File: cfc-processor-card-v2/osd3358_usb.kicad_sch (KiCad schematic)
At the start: 33 parts, among them U7 OSD3358-512M-BSM, Y1 24MHz, Y2 ABS07-32.768KHZ-T

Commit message: Clean up CFC Processor Card from Scott's initial import which was Gerber identical to origianl EAGLE schematic. Interestingly, this version was already changed for the v2 backplane which is great. Align schematic to be more KiCAD like based off of the C3, rename a few things, remove some outdated OPD connections, import sch into pcb, clean up pcb detritus, and import DRU settings. No longer Gerber identicial, but it's now ready for further polishing for fabrication.
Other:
- note removed: "1.2"
- note removed: "OreSat Star Tracker: USB, JTAG, OSC"
- company: (none) -> Portland State Aerospace Society
- title: (none) -> OreSat CFC Processor Card
- moved on the sheet: C19, C22, C29, C30, C50, C51, FB2, R13, R21, R27, TP10, TP11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

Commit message: more trace polishing.
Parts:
- C19, C22, C29, C30, C50, C51, R13, R21, R27: footprint cfc-card:.0603-A -> oresat-passives:0603-C-NOSILK
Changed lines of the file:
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@@
 			)
 		)
-		(property "Footprint" "cfc-card:.0603-A"
+		(property "Footprint" "oresat-passives:0603-C-NOSILK"
 			(at 153.67 80.01 0)
 			(effects
@@
 			)
 		)
-		(property "Footprint" "cfc-card:.0603-A"
+		(property "Footprint" "oresat-passives:0603-C-NOSILK"
 			(at 128.27 87.63 0)
 			(effects
@@
 			)
 		)
-		(property "Footprint" "cfc-card:.0603-A"
+		(property "Footprint" "oresat-passives:0603-C-NOSILK"
 			(at 135.89 118.11 0)
 			(effects
@@
 			)
 		)
-		(property "Footprint" "cfc-card:.0603-A"
+		(property "Footprint" "oresat-passives:0603-C-NOSILK"
 			(at 313.69 102.87 0)
 			(effects
@@
 			)
 		)
-		(property "Footprint" "cfc-card:.0603-A"
+		(property "Footprint" "oresat-passives:0603-C-NOSILK"
 			(at 135.89 102.87 0)
 			(effects
@@
 			)
 		)
-		(property "Footprint" "cfc-card:.0603-A"
+		(property "Footprint" "oresat-passives:0603-C-NOSILK"
 			(at 252.73 87.63 0)
 			(effects
@@
 			)
 		)
-		(property "Footprint" "cfc-card:.0603-A"
+		(property "Footprint" "oresat-passives:0603-C-NOSILK"
 			(at 158.75 110.49 0)
 			(effects
@@
 			)
 		)
-		(property "Footprint" "cfc-card:.0603-A"
+		(property "Footprint" "oresat-passives:0603-C-NOSILK"
 			(at 128.27 72.39 0)
 			(effects
@@
 			)
 		)
-		(property "Footprint" "cfc-card:.0603-A"
+		(property "Footprint" "oresat-passives:0603-C-NOSILK"
 			(at 313.69 95.25 0)
 			(effects

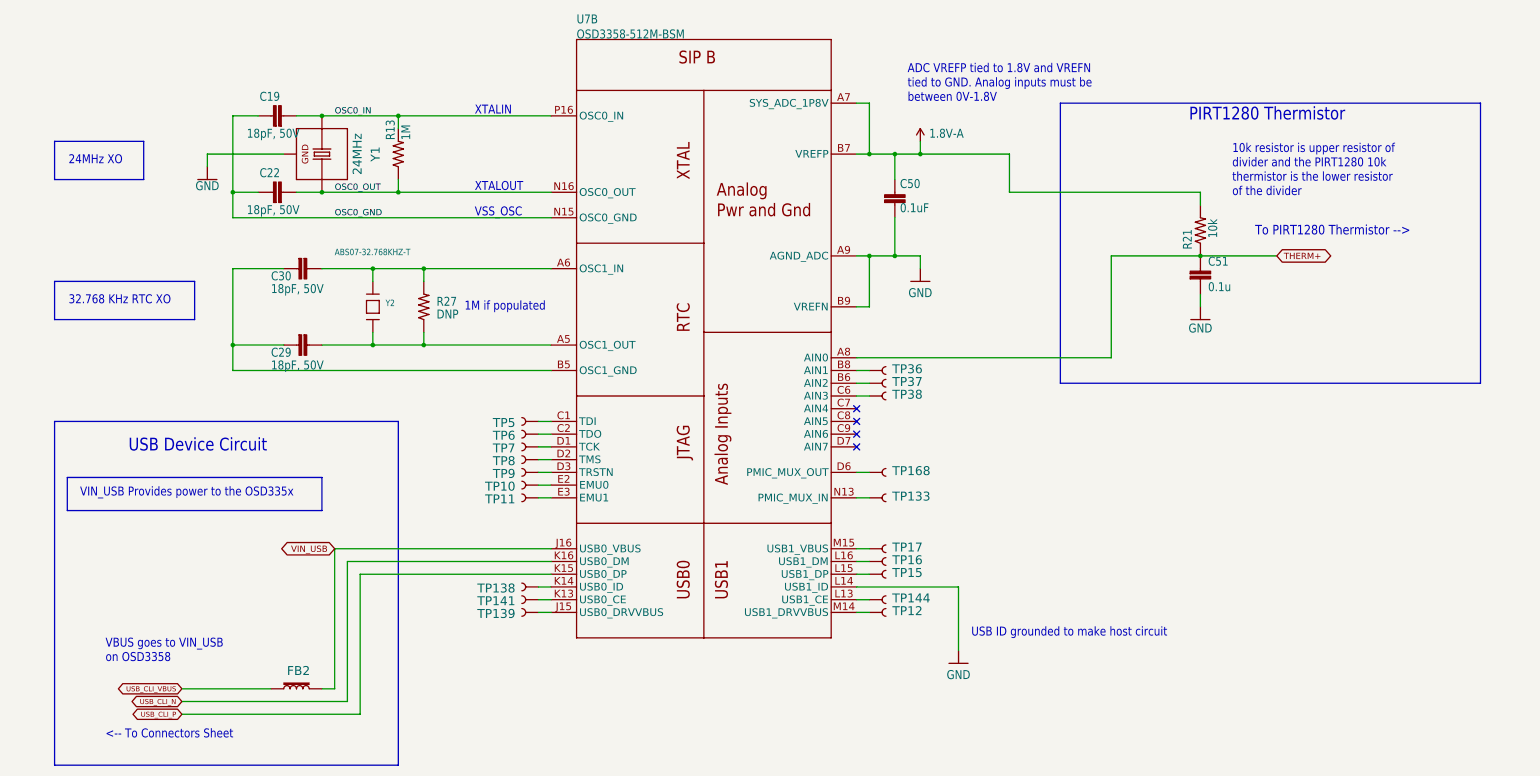
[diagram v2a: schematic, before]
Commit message: Final polish on schematic and PCB. Cleaned up BOM, fixed github issues which were not really issues. Lots of BOM cleanup, with MPNs and DPNs.
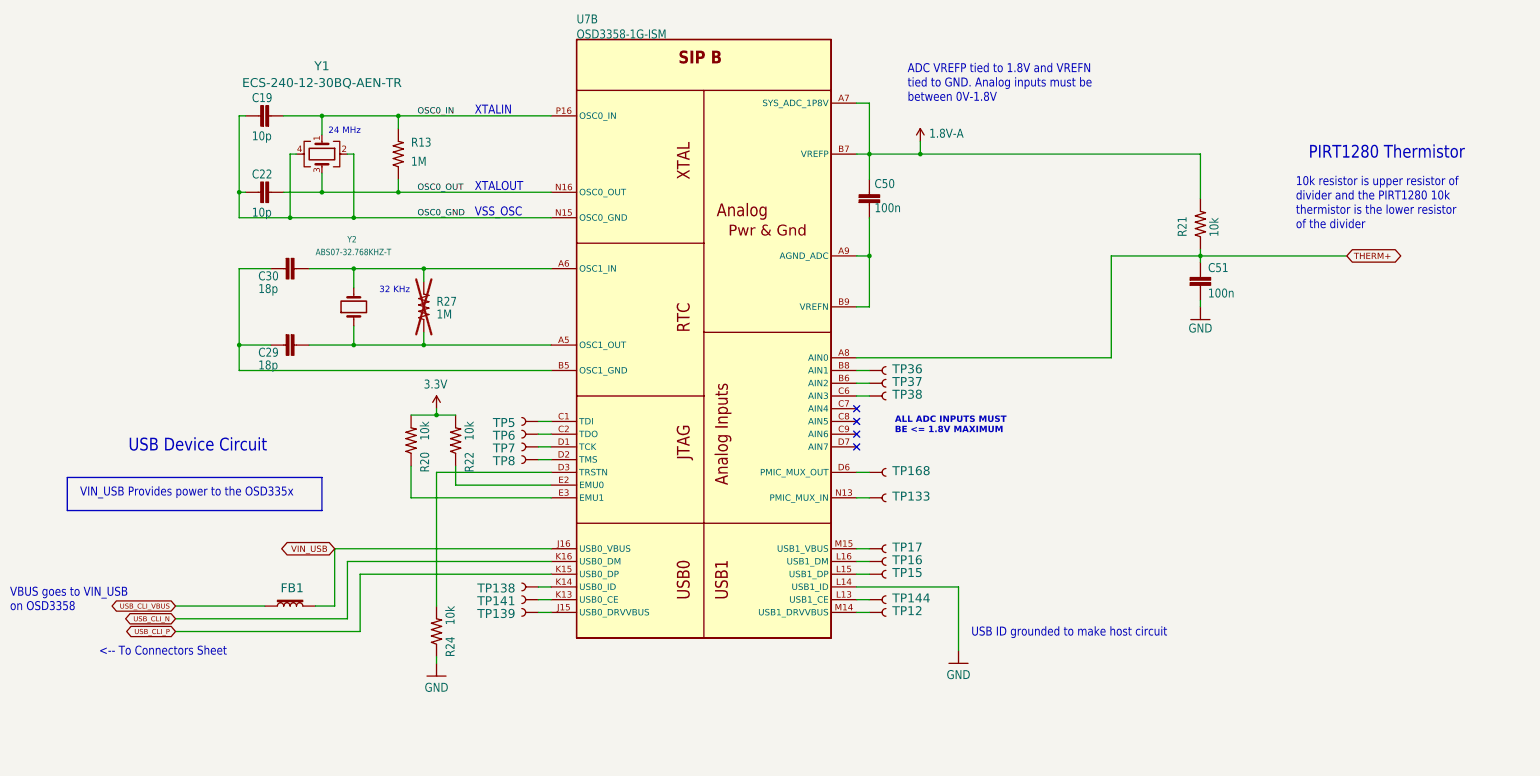
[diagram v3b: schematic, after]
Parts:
- removed TP10, TP11, TP9: TEST-POINT3X4, cfc-card:PAD.03X.04, symbol cfc-card-eagle-import:TEST-POINT3X4
- added R20, R22, R24: 10k, oresat-passives:0603-C-NOSILK, symbol cfc-card-eagle-import:R-US_0603-A
- C19, C22: value 18pF, 50V -> 10p; DIS (none) -> DigiKey; DPN (none) -> 399-6840-1-ND; MFR (none) -> KEMET; MPN (none) -> C0603C100J5GACAUTO
- C29, C30: value 18pF, 50V -> 18p; DIS (none) -> DigiKey; DPN (none) -> 399-C0603C180F5GACAUTOCT-ND; MFR (none) -> KEMET; MPN (none) -> C0603C180F5GACAUTO
- C50: value 0.1uF -> 100n; DIS (none) -> DigiKey; DPN (none) -> 587-3472-1-ND; MFR (none) -> Taiyo Yuden; MPN (none) -> TMK107BJ104KAHT
- C51: value 0.1u -> 100n; DIS (none) -> DigiKey; DPN (none) -> 587-3472-1-ND; MFR (none) -> Taiyo Yuden; MPN (none) -> TMK107BJ104KAHT
- FB1: renamed from FB2; value 30Ω/1.8A -> BLM18KG300JH1D; footprint cfc-card:0603 -> Inductor_SMD:L_0603_1608Metric; DIS (none) -> DigiKey; MFR (none) -> Murata Electronics
- R13: DIS (none) -> DigiKey; DPN (none) -> RMCF0603FG1M00CT-ND; MFR (none) -> Stackpole Electronics Inc; MPN (none) -> RMCF0603FG1M00
- R21: DIS (none) -> DigiKey; DPN (none) -> RMCF0603FT10K0CT-ND; MFR (none) -> Stackpole Electronics Inc; MPN (none) -> RMCF0603FT10K0
- R27: value DNP -> 1M; now not fitted
- TP12, TP133, TP138, TP139, TP141, TP144, TP15, TP16, TP168, TP17, TP36, TP37, TP38, TP5, TP6, TP7, TP8: now left out of the parts list
- U7: value OSD3358-512M-BSM -> OSD3358-1G-ISM; footprint cfc-card:OSD335X-BGA-256 -> oresat-ics:U-Octavo-OSD335X-BGA-256; symbol cfc-card-eagle-import:OSD3358-512M-BSM -> oresat-ics:OSD3358-512M-BSM; DIS (none) -> DigiKey; DPN (none) -> 1676-OSD3358-1G-ISM-ND; MFR (none) -> Octavo Systems; MPN (none) -> OSD3358-1G-ISM
- Y1: value 24MHz -> ECS-240-12-30BQ-AEN-TR; footprint cfc-card:5X3.2-4SMD -> oresat-passives:CRYSTAL-5X3.2-4SMD; symbol cfc-card-eagle-import:ECS-240-12-30BQ-AEN-TR -> Device:Crystal_GND24; DIS (none) -> DigiKey; DPN (none) -> XC2580CT-ND; MFR (none) -> ECS Inc; MPN (none) -> ECS-240-12-30BQ-AEN-TR
- Y2: footprint cfc-card:CRYSTAL_3.2X1.5 -> oresat-passives:CRYSTAL_3.2X1.5; symbol cfc-card-eagle-import:ABS07-32.768KHZ-T -> Device:Crystal; DIS (none) -> DigiKey; DPN (none) -> 535-9542-1-ND; MFR (none) -> Abracon LLC; MPN (none) -> ABS07-32.768KHZ-T
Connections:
- net GND: now also R24.1; no longer C50.2, U7.A9 (AGND_ADC), U7.B9 (VREFN), Y1.2 (GND), Y1.4 (GND)
- net OSC0_GND: now also Y1.2, Y1.4
- net at U7.D3 (TRSTN): now also R24.2
- net at C29.1, R27.1, U7.A5 (OSC1_OUT): now also Y2.1; no longer Y2.P$1
- net at U7.E2 (EMU0): now also R22.1
- net at U7.E3 (EMU1): now also R20.1
- net at C30.1, R27.2, U7.A6 (OSC1_IN): now also Y2.2; no longer Y2.P$2
- new net: C50.2, U7.A9 (AGND_ADC), U7.B9 (VREFN)
- new net 3.3V: R20.2, R22.2
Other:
- note added: "24 MHz"
- note added: "32 KHz"
- note added: "ALL ADC INPUTS MUST BE <= 1.8V MAXIMUM"
- note removed: "1M if populated"
- note removed: "24MHz XO"
- note removed: "32.768 KHz RTC XO"
- note removed: "To PIRT1280 Thermistor -->"
- moved on the sheet: C19, C22, C29, C30, C50, C51, FB1, R21
